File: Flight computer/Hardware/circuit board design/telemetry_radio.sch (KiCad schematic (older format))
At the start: 0 parts

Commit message: Added documentation and also the references to all components
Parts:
- added U?: Si4463, Package_DFN_QFN:QFN-20-1EP_4x4mm_P0.5mm_EP2.6x2.6mm_ThermalVias, symbol RF:Si4463
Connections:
- new net GND: U?.18 (GND), U?.21 (GND)
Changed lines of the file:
@@
 EESchema Schematic File Version 4
+LIBS:circuit board design-cache
 EELAYER 29 0
 EELAYER END
@@
 Comment4 ""
 $EndDescr
+$Comp
+L RF:Si4463 U?
+U 1 1 5D5CB5C3
+P 5900 3150
+F 0 "U?" H 5900 2361 50  0000 C CNN
+F 1 "Si4463" H 5900 2270 50  0000 C CNN
+F 2 "Package_DFN_QFN:QFN-20-1EP_4x4mm_P0.5mm_EP2.6x2.6mm_ThermalVias" H 5900 4350 50  0001 C CNN
+F 3 "https://www.silabs.com/documents/public/data-sheets/Si4464-63-61-60.pdf" H 5600 3050 50  0001 C CNN
+	1    5900 3150
+	1    0    0    -1
+$EndComp
 $EndSCHEMATC

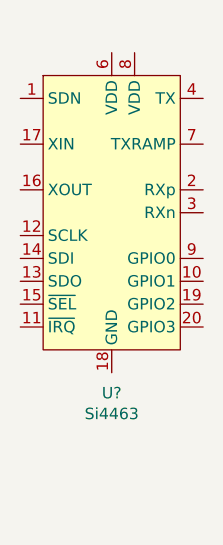
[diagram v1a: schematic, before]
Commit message: Got the GPS wired up with the MAX-M8C.
I wired up the MCU to the GPS as well. Sensors are also wired up to the I2C line.

TODO:
-make everything run on 3.3V
- work out the pyro charges and drivers
many more.
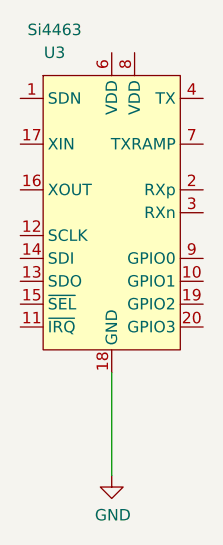
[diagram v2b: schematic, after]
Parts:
- gave numbers to parts that had none: 1
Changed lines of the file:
@@
 $EndDescr
 $Comp
-L RF:Si4463 U?
+L RF:Si4463 U3
 U 1 1 5D5CB5C3
 P 5900 3150
-F 0 "U?" H 5900 2361 50  0000 C CNN
-F 1 "Si4463" H 5900 2270 50  0000 C CNN
+F 0 "U3" H 5650 3850 50  0000 C CNN
+F 1 "Si4463" H 5650 3950 50  0000 C CNN
 F 2 "Package_DFN_QFN:QFN-20-1EP_4x4mm_P0.5mm_EP2.6x2.6mm_ThermalVias" H 5900 4350 50  0001 C CNN
 F 3 "https://www.silabs.com/documents/public/data-sheets/Si4464-63-61-60.pdf" H 5600 3050 50  0001 C CNN
@@
 	1    0    0    -1
 $EndComp
+Wire Wire Line
+	5900 3850 5900 4300
+$Comp
+L power:GND #PWR09
+U 1 1 5D5CDCF8
+P 5900 4300
+F 0 "#PWR09" H 5900 4050 50  0001 C CNN
+F 1 "GND" H 5905 4127 50  0000 C CNN
+F 2 "" H 5900 4300 50  0001 C CNN
+F 3 "" H 5900 4300 50  0001 C CNN
+	1    5900 4300
+	1    0    0    -1
+$EndComp

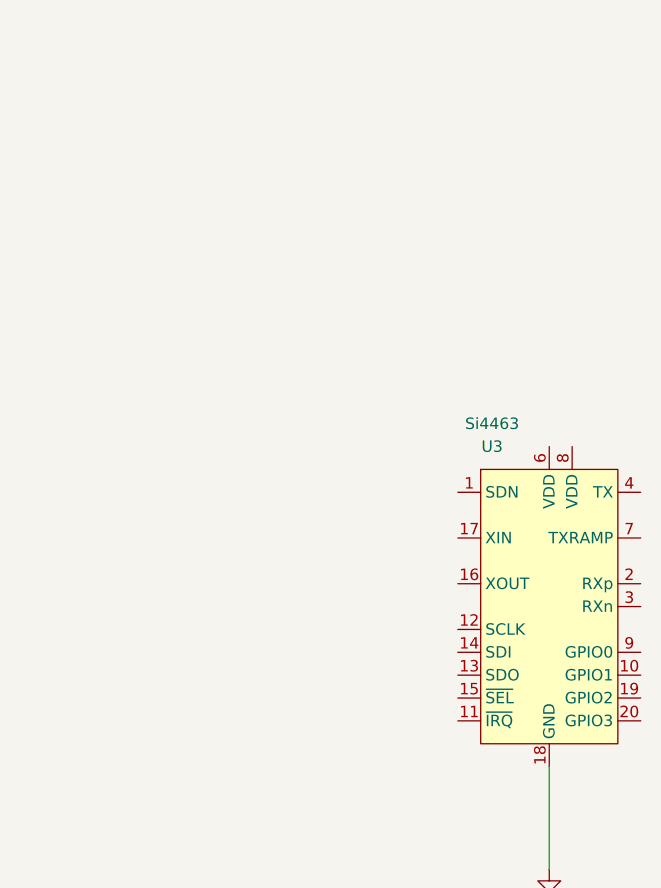
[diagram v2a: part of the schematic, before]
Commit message: Connected the SPI connection with the SIlabs radio and the XTAL
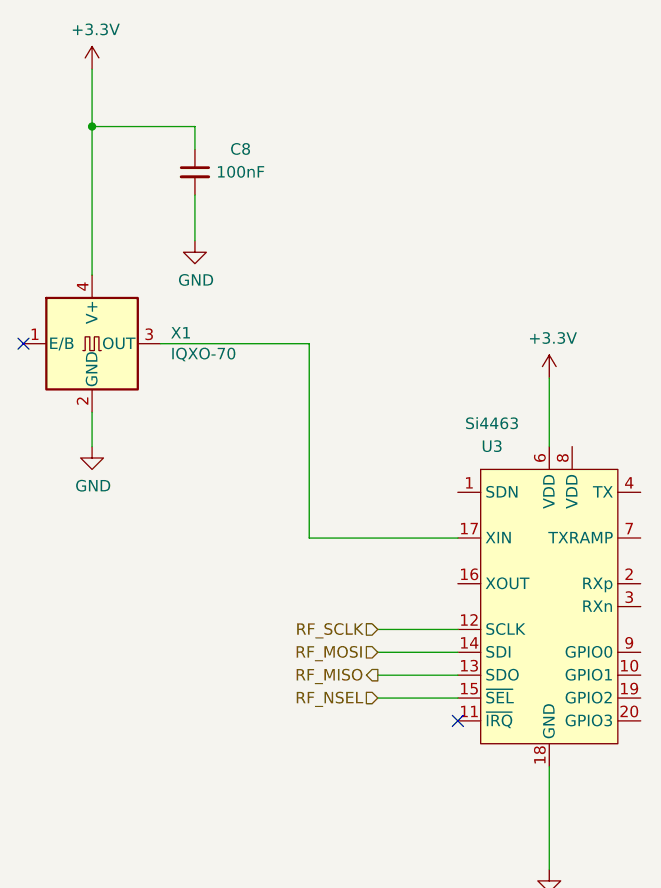
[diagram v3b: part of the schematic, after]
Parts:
- added C8: 100nF, Capacitor_SMD:C_0402_1005Metric, symbol Device:C_Small
- added X1: IQXO-70, Oscillator:Oscillator_SMD_IQD_IQXO70-4Pin_7.5x5.0mm, symbol Oscillator:IQXO-70
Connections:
- net GND: now also C8.2, X1.2 (GND)
- net RF_SCLK: now reaches U3.12 (SCLK)
- net RF_MISO: now reaches U3.13 (SDO)
- net RF_MOSI: now reaches U3.14 (SDI)
- net RF_NSEL: now reaches U3.15 (~SEL)
- net at U3.17 (XIN): now also X1.3 (OUT)
- net +3V3: now reaches U3.6 (VDD)
- net +3V3: now also C8.1, X1.4 (V+)
- no-connect marks 0 -> 2
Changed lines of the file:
@@
 $Descr A4 11693 8268
 encoding utf-8
-Sheet 6 6
+Sheet 4 6
 Title ""
 Date ""
@@
 Comment4 ""
 $EndDescr
-$Comp
-L RF:Si4463 U3
-U 1 1 5D5CB5C3
-P 5900 3150
-F 0 "U3" H 5650 3850 50  0000 C CNN
-F 1 "Si4463" H 5650 3950 50  0000 C CNN
-F 2 "Package_DFN_QFN:QFN-20-1EP_4x4mm_P0.5mm_EP2.6x2.6mm_ThermalVias" H 5900 4350 50  0001 C CNN
-F 3 "https://www.silabs.com/documents/public/data-sheets/Si4464-63-61-60.pdf" H 5600 3050 50  0001 C CNN
-	1    5900 3150
-	1    0    0    -1
-$EndComp
 Wire Wire Line
 	5900 3850 5900 4300
@@
 	1    0    0    -1
 $EndComp
+$Comp
+L Oscillator:IQXO-70 X1
+U 1 1 5D61BDEA
+P 3900 2000
+F 0 "X1" H 4244 2046 50  0000 L CNN
+F 1 "IQXO-70" H 4244 1955 50  0000 L CNN
+F 2 "Oscillator:Oscillator_SMD_IQD_IQXO70-4Pin_7.5x5.0mm" H 4575 1675 50  0001 C CNN
+F 3 "http://www.iqdfrequencyproducts.com/products/details/iqxo-70-11-30.pdf" H 3800 2000 50  0001 C CNN
+	1    3900 2000
+	1    0    0    -1
+$EndComp
+Wire Wire Line
+	4200 2000 4850 2000
+Wire Wire Line
+	4850 2850 5500 2850
+$Comp
+L power:+3.3V #PWR015
+U 1 1 5D61DCA7
+P 3900 800
+F 0 "#PWR015" H 3900 650 50  0001 C CNN
+F 1 "+3.3V" H 3915 973 50  0000 C CNN
+F 2 "" H 3900 800 50  0001 C CNN
+F 3 "" H 3900 800 50  0001 C CNN
+	1    3900 800
+	1    0    0    -1
+$EndComp
+Wire Wire Line
+	4850 2000 4850 2850
+Wire Wire Line
+	3900 1050 4350 1050
+Connection ~ 3900 1050
+Wire Wire Line
+	3900 1050 3900 1700
+$Comp
+L power:GND #PWR017
+U 1 1 5D6241AC
+P 4350 1550
+F 0 "#PWR017" H 4350 1300 50  0001 C CNN
+F 1 "GND" H 4355 1377 50  0000 C CNN
+F 2 "" H 4350 1550 50  0001 C CNN
+F 3 "" H 4350 1550 50  0001 C CNN
+	1    4350 1550
+	1    0    0    -1
+$EndComp
+$Comp
+L Device:C_Small C?
+U 1 1 5D625FA7
+P 4350 1250
+AR Path="/5D5B165E/5D625FA7" Ref="C?"  Part="1"
+AR Path="/5D5B17D8/5D625FA7" Ref="C8"  Part="1"
+F 0 "C8" H 4550 1350 50  0000 C CNN
+F 1 "100nF" H 4550 1250 50  0000 C CNN
+F 2 "Capacitor_SMD:C_0402_1005Metric" H 4350 1250 50  0001 C CNN
+F 3 "~" H 4350 1250 50  0001 C CNN
+	1    4350 1250
+	1    0    0    -1
+$EndComp
+Wire Wire Line
+	4350 1150 4350 1050
+Wire Wire Line
+	4350 1550 4350 1350
+Wire Wire Line
+	3900 800  3900 1050
+$Comp
+L power:GND #PWR016
+U 1 1 5D626EB1
+P 3900 2450
+F 0 "#PWR016" H 3900 2200 50  0001 C CNN
+F 1 "GND" H 3905 2277 50  0000 C CNN
+F 2 "" H 3900 2450 50  0001 C CNN
+F 3 "" H 3900 2450 50  0001 C CNN
+	1    3900 2450
+	1    0    0    -1
+$EndComp
+Wire Wire Line
+	3900 2450 3900 2300
+NoConn ~ 3600 2000
+Text HLabel 5150 3250 0    50   Input ~ 0
+RF_SCLK
+Wire Wire Line
+	5150 3250 5500 3250
+Text HLabel 5150 3450 0    50   Output ~ 0
+RF_MISO
+Wire Wire Line
+	5150 3450 5500 3450
+Text HLabel 5150 3350 0    50   Input ~ 0
+RF_MOSI
+Wire Wire Line
+	5150 3350 5500 3350
+Text HLabel 5150 3550 0    50   Input ~ 0
+RF_NSEL
+Wire Wire Line
+	5150 3550 5500 3550
+$Comp
+L power:+3.3V #PWR0101
+U 1 1 5D62941F
+P 5900 2150
+F 0 "#PWR0101" H 5900 2000 50  0001 C CNN
+F 1 "+3.3V" H 5915 2323 50  0000 C CNN
+F 2 "" H 5900 2150 50  0001 C CNN
+F 3 "" H 5900 2150 50  0001 C CNN
+	1    5900 2150
+	1    0    0    -1
+$EndComp
+Wire Wire Line
+	5900 2450 5900 2150
+$Comp
+L RF:Si4463 U3
+U 1 1 5D5CB5C3
+P 5900 3150
+F 0 "U3" H 5650 3850 50  0000 C CNN
+F 1 "Si4463" H 5650 3950 50  0000 C CNN
+F 2 "Package_DFN_QFN:QFN-20-1EP_4x4mm_P0.5mm_EP2.6x2.6mm_ThermalVias" H 5900 4350 50  0001 C CNN
+F 3 "https://www.silabs.com/documents/public/data-sheets/Si4464-63-61-60.pdf" H 5600 3050 50  0001 C CNN
+	1    5900 3150
+	1    0    0    -1
+$EndComp
+NoConn ~ 5500 3650
 $EndSCHEMATC

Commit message: changed boost converter resistor values for 3.3V and more
-started the pyro drivers
- connected the SPI connection between radio and MCU
- boost converter values changed.
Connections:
- no-connect marks 2 -> 13
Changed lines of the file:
@@
 $Descr A4 11693 8268
 encoding utf-8
-Sheet 4 6
+Sheet 4 7
 Title ""
 Date ""
@@
 $EndComp
 NoConn ~ 5500 3650
+NoConn ~ 6300 3650
+NoConn ~ 6300 3550
+NoConn ~ 6300 3450
+NoConn ~ 6300 3350
+NoConn ~ 6300 3150
+NoConn ~ 6300 3050
+NoConn ~ 6300 2850
+NoConn ~ 6300 2650
+NoConn ~ 5500 2650
+NoConn ~ 5500 3050
+NoConn ~ 6000 2450
 $EndSCHEMATC

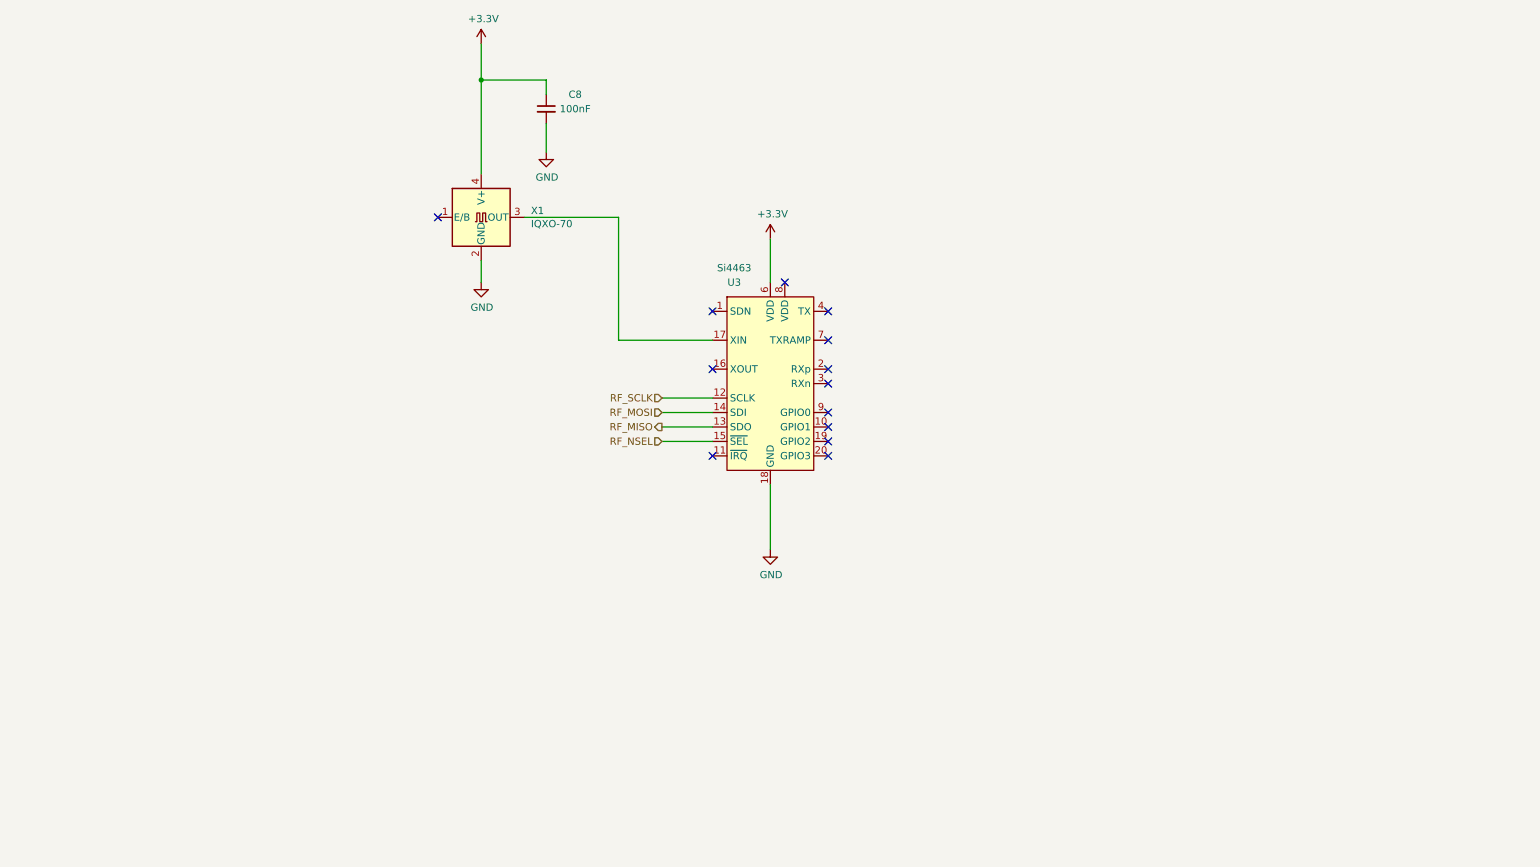
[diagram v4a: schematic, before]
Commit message: Wired up the SI4463 according to AN628 figure 16. Component values have not been set. Only type of component.
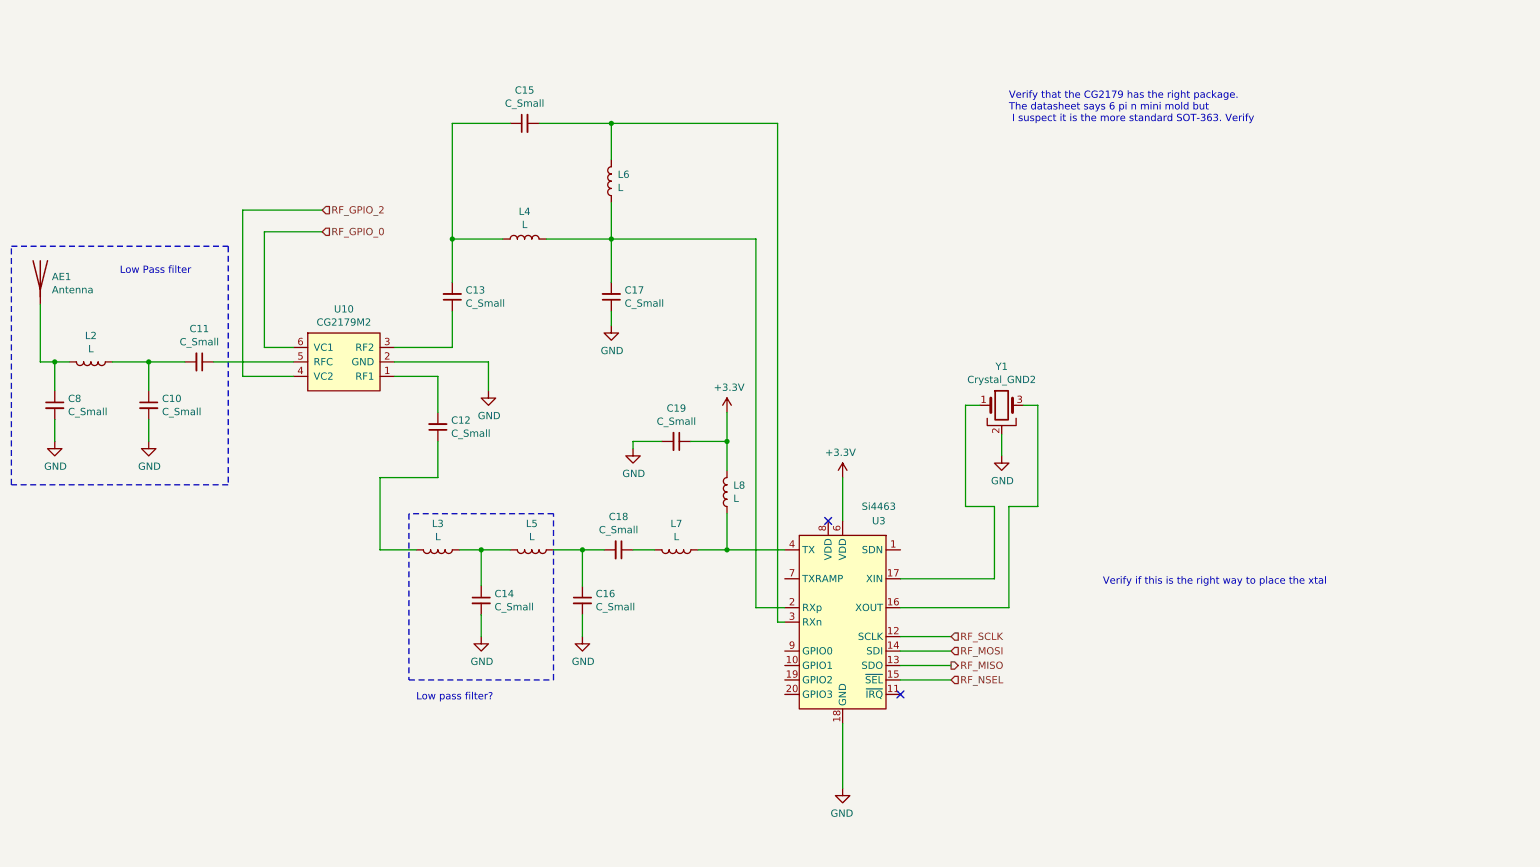
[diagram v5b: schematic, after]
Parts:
- removed X1: IQXO-70, Oscillator:Oscillator_SMD_IQD_IQXO70-4Pin_7.5x5.0mm, symbol Oscillator:IQXO-70
- added AE1: Antenna, symbol Device:Antenna
- added C10, C11, C12, C13, C14, C15, C16, C17, C18, C19: C_Small, symbol Device:C_Small
- added L2, L3, L4, L5, L6, L7, L8: L, symbol Device:L
- added U10: CG2179M2, Package_TO_SOT_SMD:SOT-363_SC-70-6_Handsoldering, symbol RF_Switch:CG2179M2
- added Y1: Crystal_GND2, symbol Device:Crystal_GND2
- C8: value 100nF -> C_Small; footprint Capacitor_SMD:C_0402_1005Metric -> (none)
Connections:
- net +3V3: now also C19.1, L8.2; no longer C8.1
- net GND: now also C10.2, C14.2, C16.2, C17.1, C19.2, U10.2 (GND), Y1.2
- net at U3.16 (XOUT): now also Y1.3
- net at U3.17 (XIN): now also Y1.1
- net at U3.2 (RXp): now also C17.2, L4.2, L6.1
- net at U3.3 (RXn): now also C15.2, L6.2
- net at U3.4 (TX): now also L7.1, L8.1
- new net: C12.2, U10.1 (RF1)
- new net: C13.1, U10.3 (RF2)
- new net: C11.1, U10.5 (RFC)
- new net: AE1.1 (A), C8.1, L2.2
- new net: C10.1, C11.2, L2.1
- new net: C18.1, L7.2
- new net: C16.1, C18.2, L5.1
- new net: C14.1, L3.1, L5.2
- new net: C12.1, L3.2
- new net: C13.2, C15.1, L4.1
- new net RF_GPIO_0: U10.6 (VC1)
- new net RF_GPIO_2: U10.4 (VC2)
- no-connect marks 13 -> 2
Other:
- note added: "Low Pass filter"
- note added: "Low pass filter?"
- note added: "Verify if this is the right way to place the xtal"
- note added: "Verify that the CG2179 has the right package. \nThe datasheet says 6 pi n mini mold but\n I suspect it is the more standard SOT-363. Verify"
- moved on the sheet: U3

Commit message: Swapped out the XTAL with a tcxo for radio.
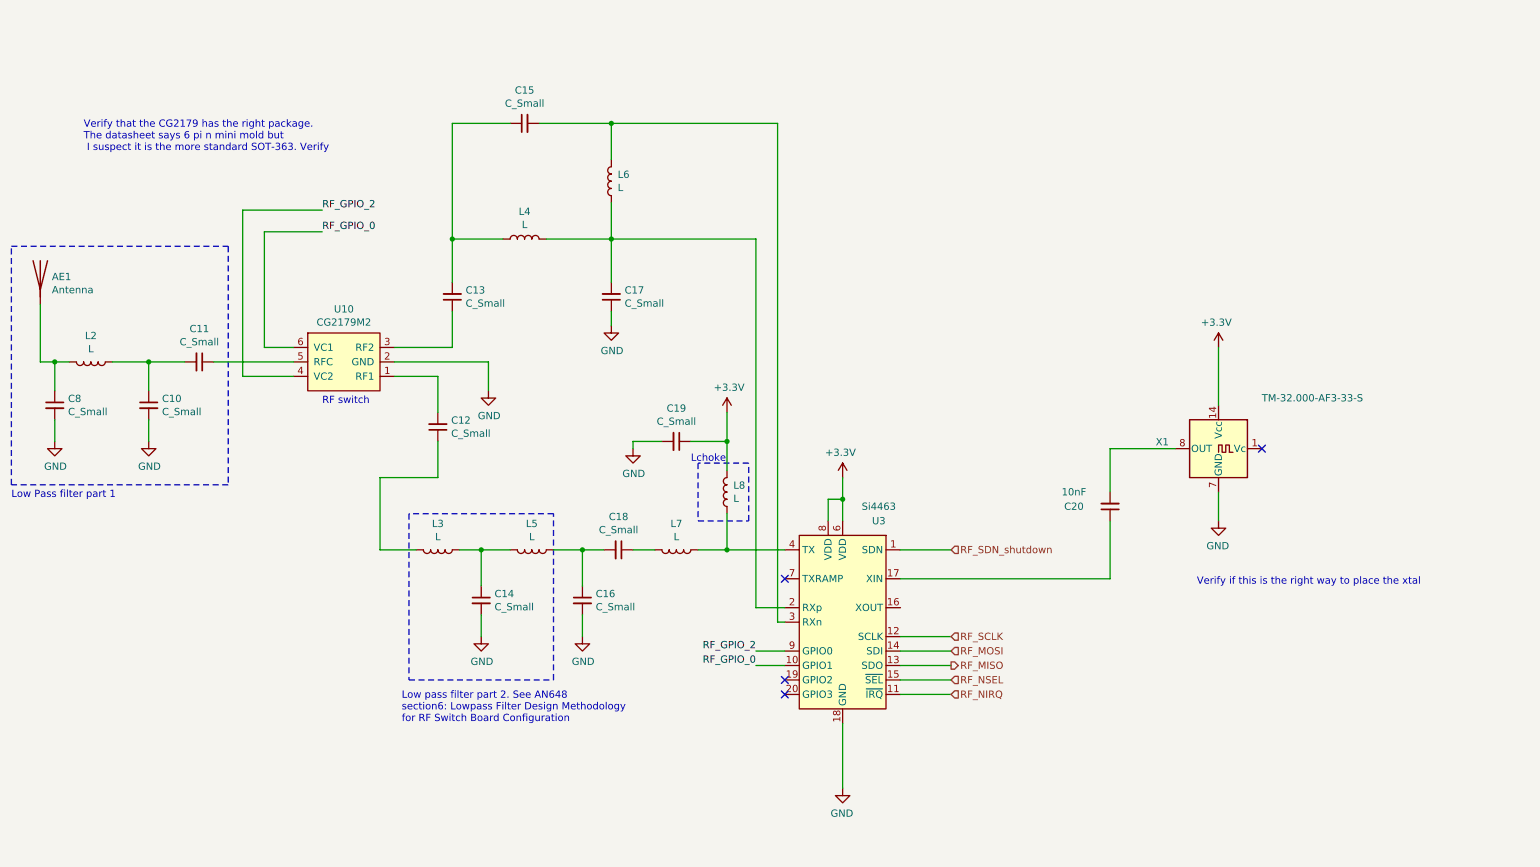
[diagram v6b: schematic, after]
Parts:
- removed Y1: Crystal_GND2, symbol Device:Crystal_GND2
- added C20: 10nF, symbol Device:C_Small
- added X1: TM-32.000-AF3-33-S, symbol Oscillator:TM-32.000-AF3-33-S
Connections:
- net +3V3: now also U3.8 (VDD), X1.14 (Vcc)
- net GND: now also X1.7 (GND)
- net RF_GPIO_0: now also U3.10 (GPIO1)
- net RF_GPIO_2: now also U3.9 (GPIO0)
- net RF_SDN_shutdown: now reaches U3.1 (SDN)
- net RF_NIRQ: now reaches U3.11 (~IRQ)
- net at U3.17 (XIN): now also C20.1
- new net: C20.2, X1.8 (OUT)
- no-connect marks 2 -> 4
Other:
- note added: "Lchoke\n"
- note added: "Low Pass filter part 1\n"
- note added: "Low pass filter part 2. See AN648\nsection6: Lowpass Filter Design Methodology \nfor RF Switch Board Configuration"
- note added: "RF switch"
- note removed: "Low Pass filter"
- note removed: "Low pass filter?"
